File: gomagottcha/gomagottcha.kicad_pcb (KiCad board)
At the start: 2 copper layers, 87 parts, among them J1 USB_B_Micro, J2 Arduino_ICSP, SW1 SW_DIP_x01, U1 BM71BLES1FC2, U10 Buzzer_490-9647-1-ND, U11 IMU, U3 MCP7381, U4 ATMEGA1284P, U5 TPS2113APWR, U6 LCD_Tomagotcha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

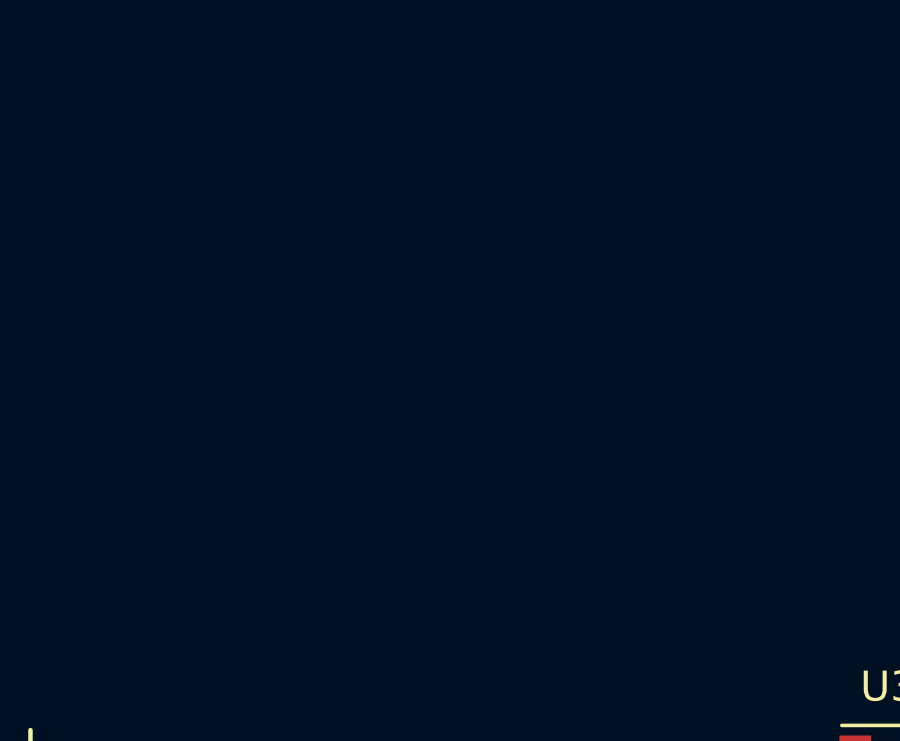
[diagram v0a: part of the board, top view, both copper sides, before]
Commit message: Footprints are done, TODO: Layout
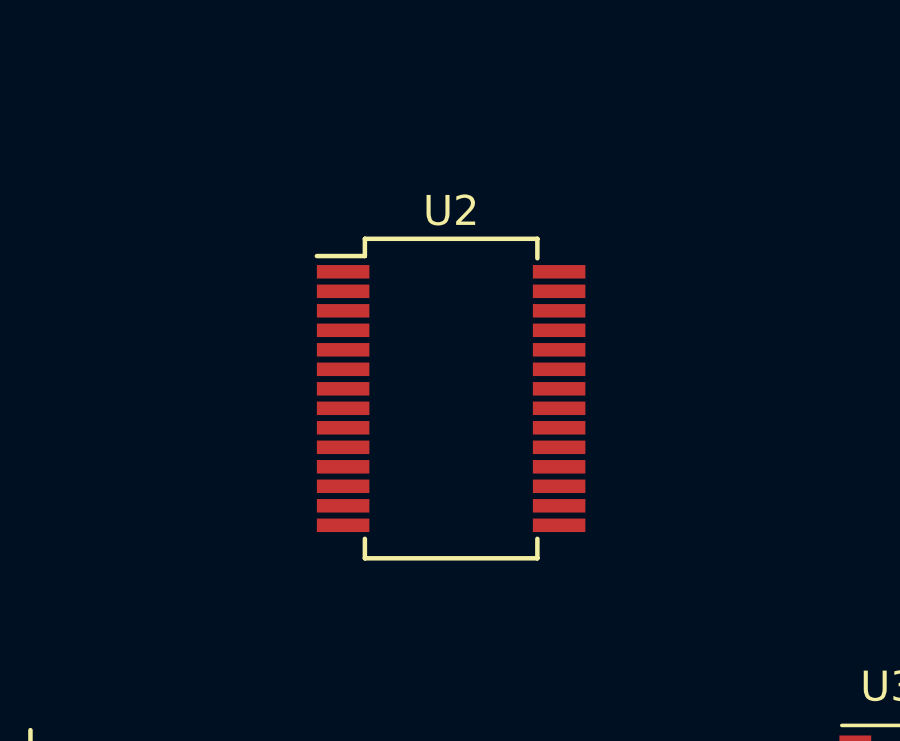
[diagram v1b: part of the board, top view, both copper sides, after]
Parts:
- added U2: FT232RL, tama-footprints:SSOP-28_5.3x10.2mm_P0.65mm, F.Cu at (103.5, 94.4)
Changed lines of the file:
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@@
     (tracks 0)
     (zones 0)
-    (modules 87)
-    (nets 92)
+    (modules 88)
+    (nets 105)
   )
   (page A4)
@@
     (solder_mask_min_width 0.25)
     (aux_axis_origin 0 0)
-    (visible_elements FFFFF77F)
+    (visible_elements 7FFFF7FF)
     (pcbplotparams
       (layerselection 0x010fc_ffffffff)
@@
   (net 90 "Net-(U1-Pad1)")
   (net 91 "Net-(J1-Pad6)")
+  (net 92 "Net-(U2-Pad3)")
+  (net 93 "Net-(U2-Pad6)")
+  (net 94 "Net-(U2-Pad8)")
+  (net 95 "Net-(U2-Pad9)")
+  (net 96 "Net-(U2-Pad10)")
+  (net 97 "Net-(U2-Pad11)")
+  (net 98 "Net-(U2-Pad12)")
+  (net 99 "Net-(U2-Pad13)")
+  (net 100 "Net-(U2-Pad14)")
+  (net 101 "Net-(U2-Pad19)")
+  (net 102 "Net-(U2-Pad24)")
+  (net 103 "Net-(U2-Pad27)")
+  (net 104 "Net-(U2-Pad28)")
   (net_class Default "This is the default net class."
     (clearance 0.2)
@@
     (add_net "Net-(U1-Pad4)")
     (add_net "Net-(U1-Pad5)")
+    (add_net "Net-(U2-Pad10)")
+    (add_net "Net-(U2-Pad11)")
+    (add_net "Net-(U2-Pad12)")
+    (add_net "Net-(U2-Pad13)")
+    (add_net "Net-(U2-Pad14)")
+    (add_net "Net-(U2-Pad19)")
+    (add_net "Net-(U2-Pad24)")
+    (add_net "Net-(U2-Pad27)")
+    (add_net "Net-(U2-Pad28)")
+    (add_net "Net-(U2-Pad3)")
+    (add_net "Net-(U2-Pad6)")
+    (add_net "Net-(U2-Pad8)")
+    (add_net "Net-(U2-Pad9)")
     (add_net "Net-(U4-Pad7)")
     (add_net "Net-(U4-Pad8)")
@@
     (add_net "Net-(U9-Pad2)")
   )
+  (module tama-footprints:SSOP-28_5.3x10.2mm_P0.65mm (layer F.Cu)
+    (at 103.505 94.361)
+    (descr "28-Lead Plastic Shrink Small Outline (SS)-5.30 mm Body [SSOP] (see Microchip Packaging Specification 00000049BS.pdf)")
+    (tags "SSOP 0.65")
+    (attr smd)
+    (fp_text reference U2 (at 0 -6.25) (layer F.SilkS)
+      (effects (font (size 1 1) (thickness 0.15)))
+    )
+    (fp_text value FT232RL (at 0 6.25) (layer F.Fab)
+      (effects (font (size 1 1) (thickness 0.15)))
+    )
+    (fp_line (start -1.65 -5.1) (end 2.65 -5.1) (layer F.Fab) (width 0.15))
+    (fp_line (start 2.65 -5.1) (end 2.65 5.1) (layer F.Fab) (width 0.15))
+    (fp_line (start 2.65 5.1) (end -2.65 5.1) (layer F.Fab) (width 0.15))
+    (fp_line (start -2.65 5.1) (end -2.65 -4.1) (layer F.Fab) (width 0.15))
+    (fp_line (start -2.65 -4.1) (end -1.65 -5.1) (layer F.Fab) (width 0.15))
+    (fp_line (start -4.75 -5.5) (end -4.75 5.5) (layer F.CrtYd) (width 0.05))
+    (fp_line (start 4.75 -5.5) (end 4.75 5.5) (layer F.CrtYd) (width 0.05))
+    (fp_line (start -4.75 -5.5) (end 4.75 -5.5) (layer F.CrtYd) (width 0.05))
+    (fp_line (start -4.75 5.5) (end 4.75 5.5) (layer F.CrtYd) (width 0.05))
+    (fp_line (start -2.875 -5.325) (end -2.875 -4.75) (layer F.SilkS) (width 0.15))
+    (fp_line (start 2.875 -5.325) (end 2.875 -4.675) (layer F.SilkS) (width 0.15))
+    (fp_line (start 2.875 5.325) (end 2.875 4.675) (layer F.SilkS) (width 0.15))
+    (fp_line (start -2.875 5.325) (end -2.875 4.675) (layer F.SilkS) (width 0.15))
+    (fp_line (start -2.875 -5.325) (end 2.875 -5.325) (layer F.SilkS) (width 0.15))
+    (fp_line (start -2.875 5.325) (end 2.875 5.325) (layer F.SilkS) (width 0.15))
+    (fp_line (start -2.875 -4.75) (end -4.475 -4.75) (layer F.SilkS) (width 0.15))
+    (fp_text user %R (at 0 0) (layer F.Fab)
+      (effects (font (size 0.8 0.8) (thickness 0.15)))
+    )
+    (pad 1 smd rect (at -3.6 -4.225) (size 1.75 0.45) (layers F.Cu F.Paste F.Mask)
+      (net 57 "Net-(R8-Pad2)"))
+    (pad 2 smd rect (at -3.6 -3.575) (size 1.75 0.45) (layers F.Cu F.Paste F.Mask)
+      (net 66 "Net-(C6-Pad2)"))
+    (pad 3 smd rect (at -3.6 -2.925) (size 1.75 0.45) (layers F.Cu F.Paste F.Mask)
+      (net 92 "Net-(U2-Pad3)"))
+    (pad 4 smd rect (at -3.6 -2.275) (size 1.75 0.45) (layers F.Cu F.Paste F.Mask)
+      (net 18 +3V3))
+    (pad 5 smd rect (at -3.6 -1.625) (size 1.75 0.45) (layers F.Cu F.Paste F.Mask)
+      (net 62 "Net-(R7-Pad2)"))
+    (pad 6 smd rect (at -3.6 -0.975) (size 1.75 0.45) (layers F.Cu F.Paste F.Mask)
+      (net 93 "Net-(U2-Pad6)"))
+    (pad 7 smd rect (at -3.6 -0.325) (size 1.75 0.45) (layers F.Cu F.Paste F.Mask)
+      (net 3 GND))
+    (pad 8 smd rect (at -3.6 0.325) (size 1.75 0.45) (layers F.Cu F.Paste F.Mask)
+      (net 94 "Net-(U2-Pad8)"))
+    (pad 9 smd rect (at -3.6 0.975) (size 1.75 0.45) (layers F.Cu F.Paste F.Mask)
+      (net 95 "Net-(U2-Pad9)"))
+    (pad 10 smd rect (at -3.6 1.625) (size 1.75 0.45) (layers F.Cu F.Paste F.Mask)
+      (net 96 "Net-(U2-Pad10)"))
+    (pad 11 smd rect (at -3.6 2.275) (size 1.75 0.45) (layers F.Cu F.Paste F.Mask)
+      (net 97 "Net-(U2-Pad11)"))
+    (pad 12 smd rect (at -3.6 2.925) (size 1.75 0.45) (layers F.Cu F.Paste F.Mask)
+      (net 98 "Net-(U2-Pad12)"))
+    (pad 13 smd rect (at -3.6 3.575) (size 1.75 0.45) (layers F.Cu F.Paste F.Mask)
+      (net 99 "Net-(U2-Pad13)"))
+    (pad 14 smd rect (at -3.6 4.225) (size 1.75 0.45) (layers F.Cu F.Paste F.Mask)
+      (net 100 "Net-(U2-Pad14)"))
+    (pad 15 smd rect (at 3.6 4.225) (size 1.75 0.45) (layers F.Cu F.Paste F.Mask)
+      (net 11 "Net-(J1-Pad3)"))
+    (pad 16 smd rect (at 3.6 3.575) (size 1.75 0.45) (layers F.Cu F.Paste F.Mask)
+      (net 13 "Net-(J1-Pad2)"))
+    (pad 17 smd rect (at 3.6 2.925) (size 1.75 0.45) (layers F.Cu F.Paste F.Mask)
+      (net 18 +3V3))
+    (pad 18 smd rect (at 3.6 2.275) (size 1.75 0.45) (layers F.Cu F.Paste F.Mask)
+      (net 3 GND))
+    (pad 19 smd rect (at 3.6 1.625) (size 1.75 0.45) (layers F.Cu F.Paste F.Mask)
+      (net 101 "Net-(U2-Pad19)"))
+    (pad 20 smd rect (at 3.6 0.975) (size 1.75 0.45) (layers F.Cu F.Paste F.Mask)
+      (net 18 +3V3))
+    (pad 21 smd rect (at 3.6 0.325) (size 1.75 0.45) (layers F.Cu F.Paste F.Mask)
+      (net 3 GND))
+    (pad 22 smd rect (at 3.6 -0.325) (size 1.75 0.45) (layers F.Cu F.Paste F.Mask)
+      (net 56 "Net-(R9-Pad2)"))
+    (pad 23 smd rect (at 3.6 -0.975) (size 1.75 0.45) (layers F.Cu F.Paste F.Mask)
+      (net 64 "Net-(R4-Pad2)"))
+    (pad 24 smd rect (at 3.6 -1.625) (size 1.75 0.45) (layers F.Cu F.Paste F.Mask)
+      (net 102 "Net-(U2-Pad24)"))
+    (pad 25 smd rect (at 3.6 -2.275) (size 1.75 0.45) (layers F.Cu F.Paste F.Mask)
+      (net 3 GND))
+    (pad 26 smd rect (at 3.6 -2.925) (size 1.75 0.45) (layers F.Cu F.Paste F.Mask)
+      (net 3 GND))
+    (pad 27 smd rect (at 3.6 -3.575) (size 1.75 0.45) (layers F.Cu F.Paste F.Mask)
+      (net 103 "Net-(U2-Pad27)"))
+    (pad 28 smd rect (at 3.6 -4.225) (size 1.75 0.45) (layers F.Cu F.Paste F.Mask)
+      (net 104 "Net-(U2-Pad28)"))
+    (model ${KISYS3DMOD}/Package_SO.3dshapes/SSOP-28_5.3x10.2mm_P0.65mm.wrl
+      (at (xyz 0 0 0))
+      (scale (xyz 1 1 1))
+      (rotate (xyz 0 0 0))
+    )
+  )
   (module "tama-footprints:Buzzer 490-9647-1-ND" (layer F.Cu)

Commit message: started layout
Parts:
- added R26: 10k, tama-footprints:R_0603_1608Metric, F.Cu at (146.4, 123.2)
- added R27: 10k, tama-footprints:R_0603_1608Metric, F.Cu at (146.4, 121.7)
- moved S4 158.0 mm to (11.4, 124.5)
- moved S1 88.1 mm to (34.3, 78.7)
- moved S3 84.9 mm to (44.5, 78.7)
- moved S2 84.7 mm to (54.6, 78.7)
- moved U4 41.2 mm to (130.8, 160.0)
- moved U1 39.1 mm to (86.2, 139.5), turned to 90 degrees
- moved U2 34.8 mm to (134.6, 78.7)
- moved J1 33.6 mm to (80.1, 151.5)
- moved SW1 22.1 mm to (92.7, 80.0)
- moved U6 4.90 mm to (62.4, 73.2)
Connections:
- C5 pad 2: Net-(C5-Pad2) -> GND
- D2 pad 1: Net-(C5-Pad2) -> Net-(D2-Pad1)
- R2 pad 2: Net-(C5-Pad2) -> Net-(D2-Pad1)
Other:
- net class Default: trace_width 0.25 -> 0.2; via_dia 0.8 -> 0.4; via_drill 0.4 -> 0.3

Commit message: REVERT TO THIS IF REPINNING DOESNT WORK
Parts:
- removed U?N1, U?N2, U?N3, U?P1, U?P2, U?P3: MOSNP, tama-footprints:SOT-363_SC-70-6
- added U12: VMotor1670-1000-ND, tama-footprints:VMotor 1670-1000-ND, F.Cu at (129.8, 49.5)
- added U13: Buzzer_490-9647-1-ND, tama-footprints:Buzzer 490-9647-1-ND, F.Cu at (94.5, 38.6)
- added U14: IMU, tama-footprints:IMU, F.Cu at (85.1, 29.1)
- BT1: footprint tama-footprints:battery_holder -> tama-footprints:PhoenixContact_MSTBVA_2,5_2-G_1x02_P5.00mm_Vertical
- C5: value 10uF -> 0.1uF
- C6: value 0.1uF -> 10uF
- R20, R23: value 1k -> 10k
- R21, R25: value 10k -> 1k
- U10: value Buzzer_490-9647-1-ND -> VMotor1670-1000-ND; footprint tama-footprints:Buzzer 490-9647-1-ND -> tama-footprints:VMotor 1670-1000-ND
- U11: value IMU -> MOSNP; footprint tama-footprints:IMU -> tama-footprints:SOT-363_SC-70-6
- U4: value ATMEGA1284P -> MOSNP; footprint tama-footprints:TQFP-44_10x10mm_P0.8mm -> tama-footprints:SOT-363_SC-70-6
- U5: value TPS2113APWR -> ATMEGA1284P; footprint tama-footprints:VSON-8_3.1x3.1mm_P0.65mm -> tama-footprints:TQFP-44_10x10mm_P0.8mm
- U6: value LCD_Tomagotcha -> TPS2113APWR; footprint tama-footprints:LCD NHD-C12864LZ-FSW-FBW-3V3-ND -> tama-footprints:TSSOP-8_4.4x3mm_P0.65mm
- U7: value MCP1700 -> MOSNP; footprint Package_TO_SOT_SMD:SOT-23 -> tama-footprints:SOT-363_SC-70-6
- U8: value VMotor1670-1000-ND -> LCD_Tomagotcha; footprint tama-footprints:VMotor 1670-1000-ND -> tama-footprints:LCD NHD-C12864LZ-FSW-FBW-3V3-ND
- U9: value VMotor1670-1000-ND -> MCP1700; footprint tama-footprints:VMotor 1670-1000-ND -> Package_TO_SOT_SMD:SOT-23
- moved BT1 228.5 mm to (41.9, 94.0)
- moved J2 181.9 mm to (90.9, 70.2), turned to 90 degrees
- moved D1 173.3 mm to (57.4, 29.5), turned to 270 degrees
- moved D3 170.1 mm to (58.3, 42.0)
- moved D4 164.4 mm to (55.2, 43.2), turned to 90 degrees
- moved C23 138.0 mm to (45.7, 28.2), turned to 90 degrees
- moved C4 134.4 mm to (45.3, 34.4), turned to 270 degrees
- moved R5 133.0 mm to (56.4, 81.3), turned to 90 degrees
- moved R6 131.3 mm to (57.1, 78.4)
- moved R15 128.1 mm to (52.7, 39.6)
- moved R25 126.5 mm to (65.2, 26.5)
- moved J1 124.8 mm to (39.1, 33.7)
- moved C3 124.6 mm to (58.3, 39.7)
- moved R14 124.2 mm to (52.7, 36.7), turned to 180 degrees
- moved C24 121.7 mm to (52.1, 28.8), turned to 270 degrees
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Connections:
- C5 pad 1: +3V3 -> /RESET
- C5 pad 2: GND -> Net-(C5-Pad2)
- C6 pad 1: /RESET -> +3V3
- C6 pad 2: Net-(C6-Pad2) -> GND
- R19 pad 1: /PC4 -> /SDA
- R20 pad 1: GND -> /PC4
- R20 pad 2: Net-(D5-Pad1) -> +3V3
- R21 pad 2: /PWM_2 -> Net-(D5-Pad1)
- R22 pad 1: GND -> /SCL
- R22 pad 2: /BUTTON1 -> +3V3
- R23 pad 1: Net-(D6-Pad1) -> GND
- R23 pad 2: GND -> /PWM_2
- R24 pad 2: /BUTTON2 -> /BUTTON1
- R25 pad 1: GND -> Net-(D6-Pad1)
- R25 pad 2: /BUTTON3 -> GND
- R26 pad 1: /SDA -> GND
- R26 pad 2: +3V3 -> /BUTTON2
- R27 pad 1: /SCL -> GND
- R27 pad 2: +3V3 -> /BUTTON3
- U10 pad 1: /Buzzer -> Net-(BT1-Pad1)
- U10 pad 2: GND -> Net-(U10-Pad2)
- U11 pad 1: /SCL -> Net-(U11-Pad1)
- U11 pad 2: +3V3 -> /PWM_2
- U11 pad 3: +3V3 -> Net-(BT1-Pad1)
- U11 pad 4: /SDA -> Net-(U11-Pad1)
- U11 pad 5: Net-(C28-Pad1) -> Net-(BT1-Pad1)
- U2 pad 2: Net-(C6-Pad2) -> Net-(C5-Pad2)
- U4 pad 1: /MOSI -> Net-(R10-Pad1)
- U4 pad 2: /MISO -> /MEAS_BAT
- U4 pad 3: /SCK -> Net-(R5-Pad1)
- U4 pad 4: /RESET -> Net-(BT1-Pad1)
- U4 pad 5: +3V3 -> Net-(R10-Pad1)
- U5 pad 1: Net-(U5-Pad1) -> /MOSI
- U5 pad 2: GND -> /MISO
- U5 pad 3: Net-(R13-Pad1) -> /SCK
- U5 pad 4: Net-(R15-Pad1) -> /RESET
- U5 pad 5: GND -> +3V3
- U5 pad 6: Net-(SW1-Pad1) -> GND
- U5 pad 7: Net-(C23-Pad1) -> Net-(U5-Pad7)
- U5 pad 8: Net-(C4-Pad1) -> Net-(U5-Pad8)
- U5 pad 9: (no net) -> Net-(R8-Pad1)
- U6 pad 1: /CS1 -> Net-(U6-Pad1)
- U6 pad 2: /PC4 -> GND
- U6 pad 3: /PB3 -> Net-(R13-Pad1)
- U6 pad 4: /WR -> Net-(R15-Pad1)
- U6 pad 5: /RD -> GND
- U6 pad 6: Net-(U6-Pad6) -> Net-(SW1-Pad1)
- U6 pad 7: Net-(U6-Pad7) -> Net-(C23-Pad1)
- U6 pad 8: Net-(U6-Pad8) -> Net-(C4-Pad1)
- U7 pad 1: GND -> Net-(U10-Pad2)
- U7 pad 2: +3V3 -> /PWM_1
- U7 pad 3: Net-(C23-Pad1) -> Net-(BT1-Pad1)
- U8 pad 1: Net-(BT1-Pad1) -> /CS1
- U8 pad 2: Net-(U8-Pad2) -> /PC4
- U9 pad 1: Net-(BT1-Pad1) -> GND
- U9 pad 2: Net-(U9-Pad2) -> +3V3
- Y1 pad 1: Net-(U4-Pad7) -> Net-(U5-Pad7)
- Y1 pad 3: Net-(U4-Pad8) -> Net-(U5-Pad8)
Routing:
- net +3V3: track 0.00 -> 242.1 mm, vias 0 -> 4
- net GND: track 0.00 -> 144.1 mm, vias 0 -> 31
- net Net-(BT1-Pad1): track 0.00 -> 91.6 mm
- net /PWM_1: track 0.00 -> 67.0 mm, vias 0 -> 2
- net /PB0: track 0.00 -> 66.1 mm, vias 0 -> 2
- net /PB1: track 0.00 -> 65.9 mm, vias 0 -> 2
- net /MEAS_BAT: track 0.00 -> 59.3 mm, vias 0 -> 2
- net Net-(SW1-Pad1): track 0.00 -> 56.3 mm, vias 0 -> 1
- net /BUTTON2: track 0.00 -> 55.3 mm, vias 0 -> 2
- net Net-(R7-Pad1): track 0.00 -> 46.0 mm, vias 0 -> 4
- net /CS1: track 0.00 -> 44.5 mm, vias 0 -> 1
- net Net-(R8-Pad1): track 0.00 -> 43.5 mm, vias 0 -> 4
- net /RX_IND: track 0.00 -> 43.1 mm, vias 0 -> 4
- net /PB2: track 0.00 -> 42.3 mm, vias 0 -> 2
- net /PB3: track 0.00 -> 40.0 mm, vias 0 -> 2
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- added copper zone on F.Cu, net +3V3
- added copper zone on B.Cu, net GND
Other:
- board outline added: 95 x 95 mm

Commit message: TODO: Add screw holes and maybe picture
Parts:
- moved C12 131.8 mm to (41.7, 53.1)
- moved C18 115.0 mm to (41.7, 55.2)
- moved R27 95.3 mm to (78.4, 83.1), turned to 270 degrees
- moved R26 84.1 mm to (88.4, 80.9), turned to 180 degrees
- moved BT1 80.8 mm to (121.9, 82.5)
- moved R10 71.2 mm to (126.7, 73.9)
- moved R11 71.2 mm to (128.8, 67.3)
- moved R5 71.2 mm to (126.2, 67.3)
- moved R6 71.2 mm to (127.0, 64.4)
- moved U4 71.2 mm to (127.8, 70.9)
- moved D5 53.4 mm to (110.2, 49.0), turned to 225 degrees
- moved R24 45.6 mm to (104.0, 83.8), turned to 180 degrees
- moved C27 42.8 mm to (128.3, 46.4), turned to 90 degrees
- moved R21 41.7 mm to (112.3, 45.6), turned to 270 degrees
- moved C25 37.7 mm to (130.4, 46.4), turned to 90 degrees
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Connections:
- R20 pad 1: /PC4 -> /RES
- U14 pad 11: /PB1 -> /DRDY_MAG
- U14 pad 12: /PB0 -> /INT_XL
- U14 pad 7: /PB2 -> /INT_MAG
- U5 pad 13: /PWM_1 -> Net-(U5-Pad13)
- U5 pad 15: /BUTTON1 -> /INT_MAG
- U5 pad 21: /RD -> /INT_XL
- U5 pad 22: /CS1 -> /DRDY_MAG
- U5 pad 23: /PC4 -> Net-(U5-Pad23)
- U5 pad 24: /WR -> /PWM_1
- U5 pad 26: /BUTTON2 -> Net-(U5-Pad26)
- U5 pad 30: /A7 -> /RD
- U5 pad 31: /A6 -> /WR
- U5 pad 32: /RX_IND -> /A0
- U5 pad 33: /RTS -> /RES
- U5 pad 34: /RST_N -> /CS1
- U5 pad 35: /CTS -> /BUTTON1
- U5 pad 36: /BUTTON3 -> /BUTTON2
- U5 pad 40: /PB0 -> /BUTTON3
- U5 pad 41: /PB1 -> /CTS
- U5 pad 42: /PB2 -> /RST_N
- U5 pad 43: /PB3 -> /RTS
- U5 pad 44: /SS -> /RX_IND
- U8 pad 2: /PC4 -> /RES
- U8 pad 3: /PB3 -> /A0
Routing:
- net Net-(BT1-Pad1): track 91.6 -> 188.0 mm
- net /PB0: track 66.1 -> 0.00 mm, vias 2 -> 0
- net /PB1: track 65.9 -> 0.00 mm, vias 2 -> 0
- net +3V3: track 242.1 -> 303.1 mm, vias 4 -> 8
- net /RESET: track 34.2 -> 92.4 mm, vias 2 -> 5
- net /PB2: track 42.3 -> 0.00 mm, vias 2 -> 0
- net /PB3: track 40.0 -> 0.00 mm, vias 2 -> 0
- net /DRDY_MAG: track 0.00 -> 36.3 mm
- net /INT_XL: track 0.00 -> 36.1 mm
- net /BUTTON3: track 31.7 -> 66.2 mm, vias 2 -> 0
- net /BUTTON1: track 0.00 -> 29.8 mm
- net /PC4: track 29.5 -> 0.00 mm, vias 2 -> 0
- net /INT_MAG: track 0.00 -> 28.7 mm
- net /CS1: track 44.5 -> 17.7 mm, vias 1 -> 0
- net /VBAT: track 2.13 -> 26.4 mm, vias 0 -> 2
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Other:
- board size 95 x 95 mm -> 95 x 68.8 mm

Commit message: added screw holes
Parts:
- added REF**: MountingHole_4mm_Pad, MountingHole:MountingHole_4mm_Pad, F.Cu at (59.7, 86.4)
- added REF**: MountingHole_4mm_Pad, MountingHole:MountingHole_4mm_Pad, F.Cu at (46.4, 19.1)
- added REF**: MountingHole_4mm_Pad, MountingHole:MountingHole_4mm_Pad, F.Cu at (123.8, 19.1)
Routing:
- net Net-(BT1-Pad1): track 188.0 -> 189.3 mm
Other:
- board size 95 x 68.8 mm -> 95.1 x 78.8 mm
